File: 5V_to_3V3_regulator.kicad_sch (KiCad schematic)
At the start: 4 parts, among them U5 TPS62162DSG

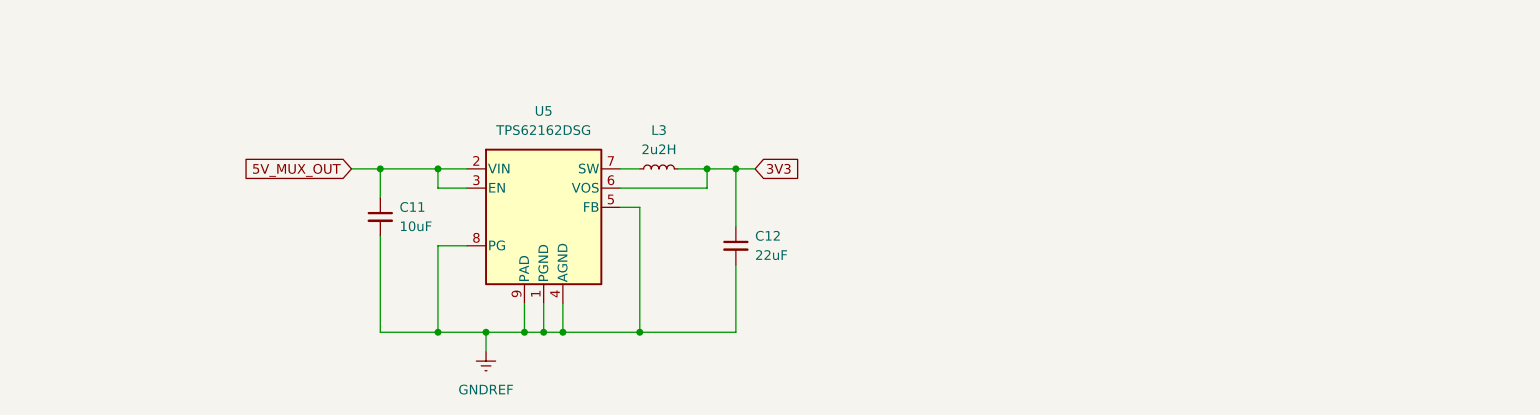
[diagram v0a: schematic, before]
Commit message: updated components and nets
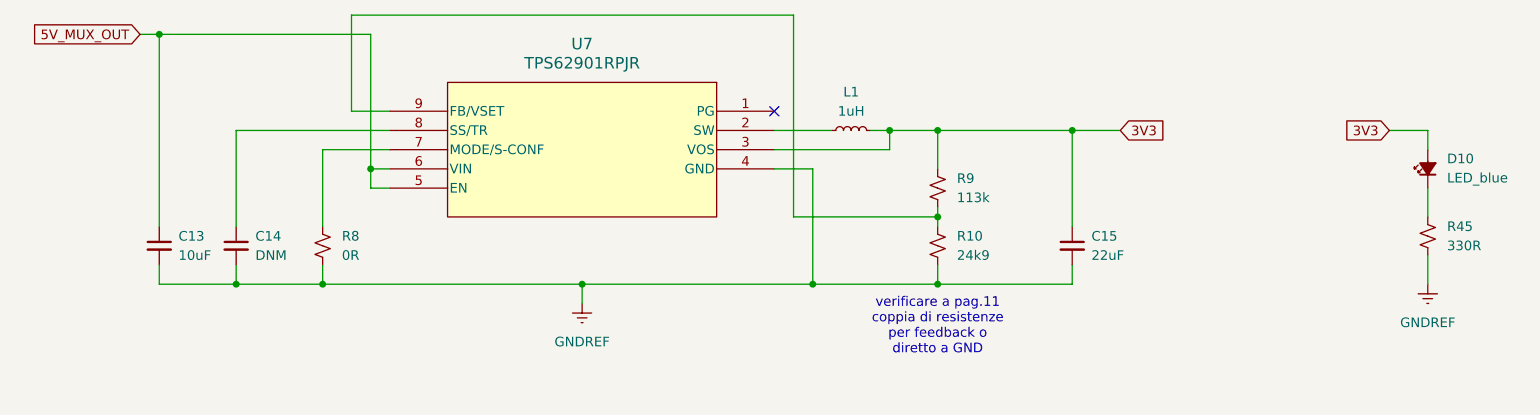
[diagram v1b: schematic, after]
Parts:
- removed C11: 10uF, symbol Device:C_Small
- removed C12: 22uF, symbol Device:C_Small
- removed L3: 2u2H, symbol Device:L_Small
- removed U5: TPS62162DSG, Package_SON:WSON-8-1EP_2x2mm_P0.5mm_EP0.9x1.6mm_ThermalVias, symbol Regulator_Switching:TPS62162DSG
- added C13: 10uF, symbol Device:C_Small
- added C14: DNM, symbol Device:C_Small
- added C15: 22uF, symbol Device:C_Small
- added D10: LED_blue, symbol Device:LED_Small_Filled
- added L1: 1uH, symbol Device:L_Small
- added R10: 24k9, symbol Device:R_Small_US
- added R45: 330R, symbol Device:R_Small_US
- added R8: 0R, symbol Device:R_Small_US
- added R9: 113k, symbol Device:R_Small_US
- added U7: TPS62901RPJR, QFN_902RPJR_TEX, symbol Regulator_Switching:TPS62901RPJR
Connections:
- net 3V3: now also C15.1, D10.2 (A), L1.2, R9.1, U7.3 (VOS)
- net 5V_MUX_OUT: now also C13.1, U7.5 (EN), U7.6 (VIN)
- net GNDREF: now also C13.2, C14.2, C15.2, R10.2, R45.2, R8.2, U7.4 (GND)
- new net: R8.1, U7.7 (MODE/S-CONF)
- new net: D10.1 (K), R45.1
- new net: L1.1, U7.2 (SW)
- new net: C14.1, U7.8 (SS/TR)
- new net: R10.1, R9.2, U7.9 (FB/VSET)
- no-connect marks 0 -> 1
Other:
- note added: "verificare a pag.11 coppia di resistenze per feedback o diretto a GND"
